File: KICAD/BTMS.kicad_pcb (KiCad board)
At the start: 4 copper layers, 76.2 x 55.1 mm, 151 parts, among them J1 Batt_Ballance, J2 AUX_Charge, J3 Battery_IO, J4 Power_Out, J5 BT_LM62, J6 DSKY, J7 PWR_SW, J8 ICSP, J9 Heater, P1 USB_C_Plug, Q1 SSM3K341R, Q2 DMN65D8L, Q3 SSM3K341R, Q4 FDN340P, Q5 FDN340P, Q6 FDN340P, Q7 DMN65D8L, Q8 DMN65D8L, U1 ACS711xLCTR-25AB, U10 BA033CC0FP-E2, U11 AON7522E, U12 AON7522E, U13 LM62CIM3/NOPB, U14 FAN3100TSX, U15 FAN3100TSX, U16 AON7522E, U17 dsPIC30F3011-PT, U18 FT230XQ, U2 AP33771, U3 IS281-4, U4 Q294700DSGR, U5 SCF4030-12-0X, U6 AONR21321, U7 ACS711xLCTR-25AB, U8 IS281-4, U9 IRS2184

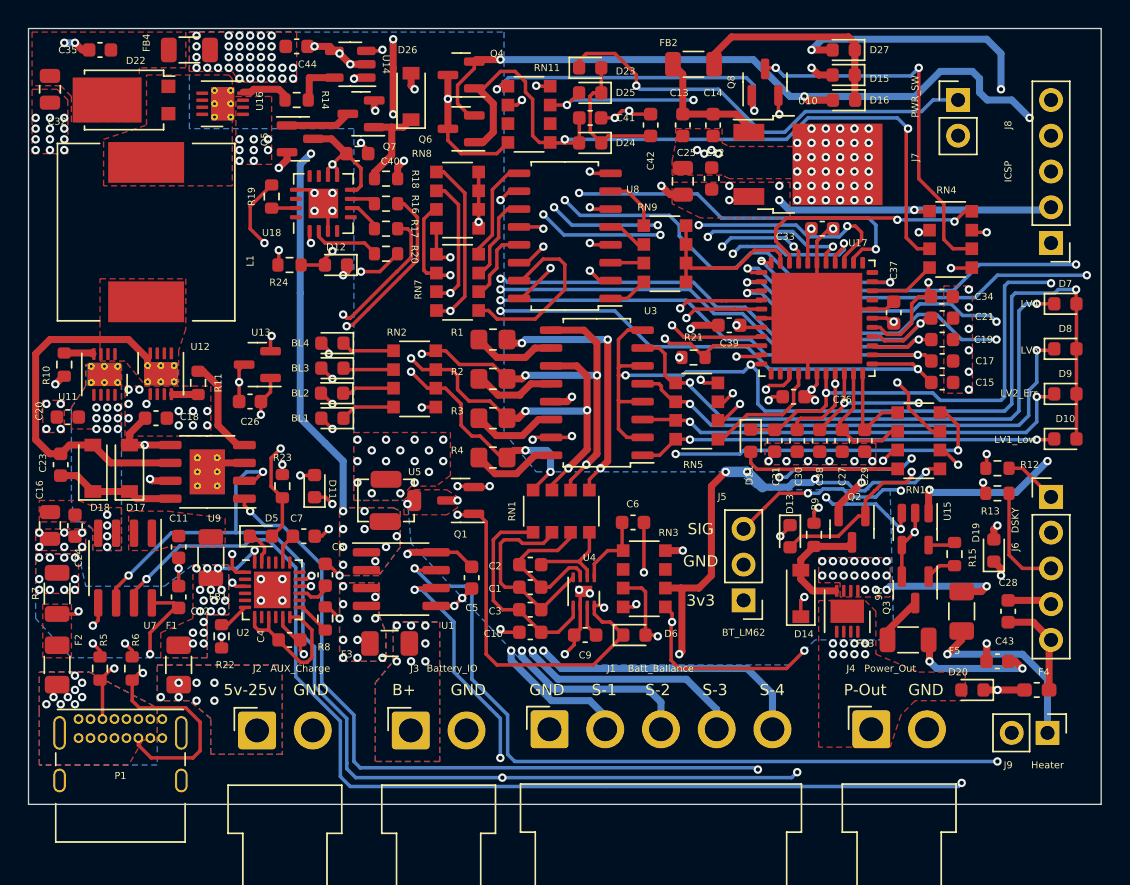
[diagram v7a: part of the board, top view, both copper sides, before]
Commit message: Added backside ground planes.
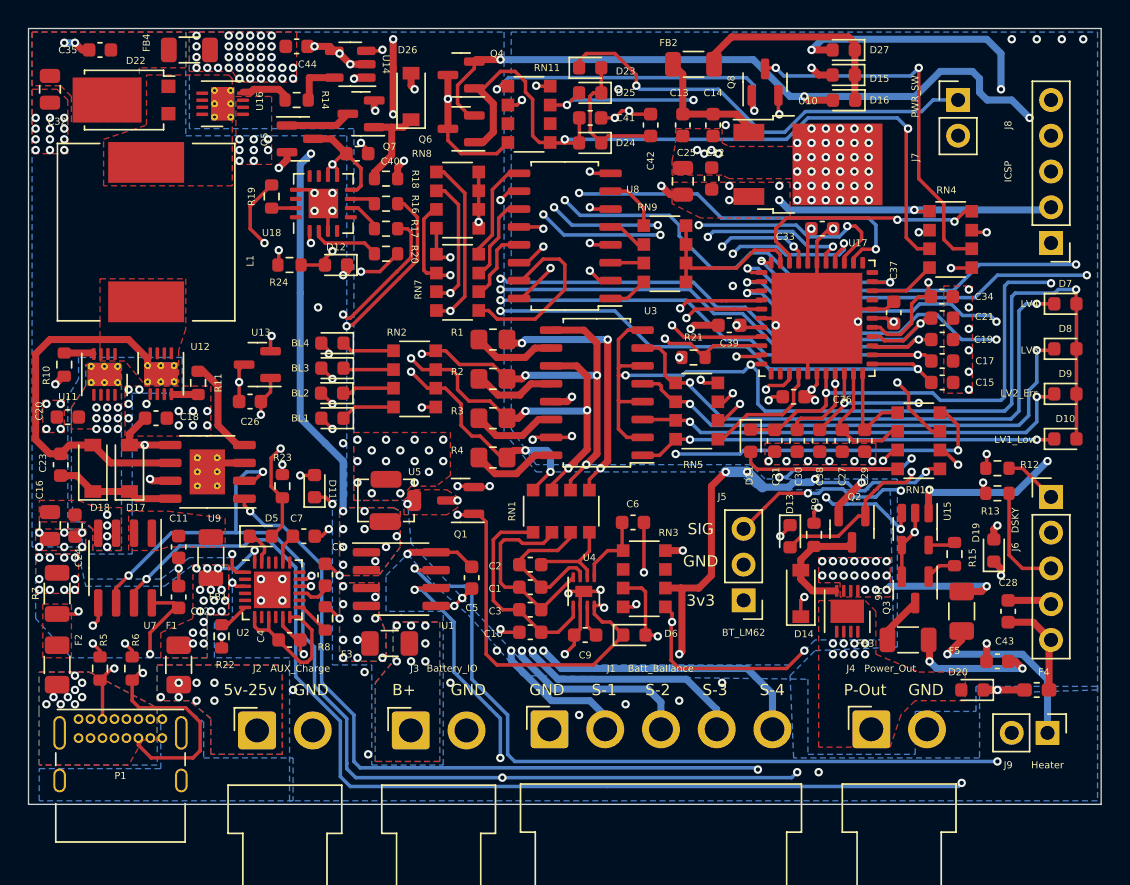
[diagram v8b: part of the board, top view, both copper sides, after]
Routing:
- net GND: track 106.8 -> 109.2 mm, vias 147 -> 168
- added copper zone on B.Cu, net GND
